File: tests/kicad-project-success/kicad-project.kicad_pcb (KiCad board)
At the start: 2 copper layers, 65 x 45 mm, 3 parts, among them SW101 SW_Push

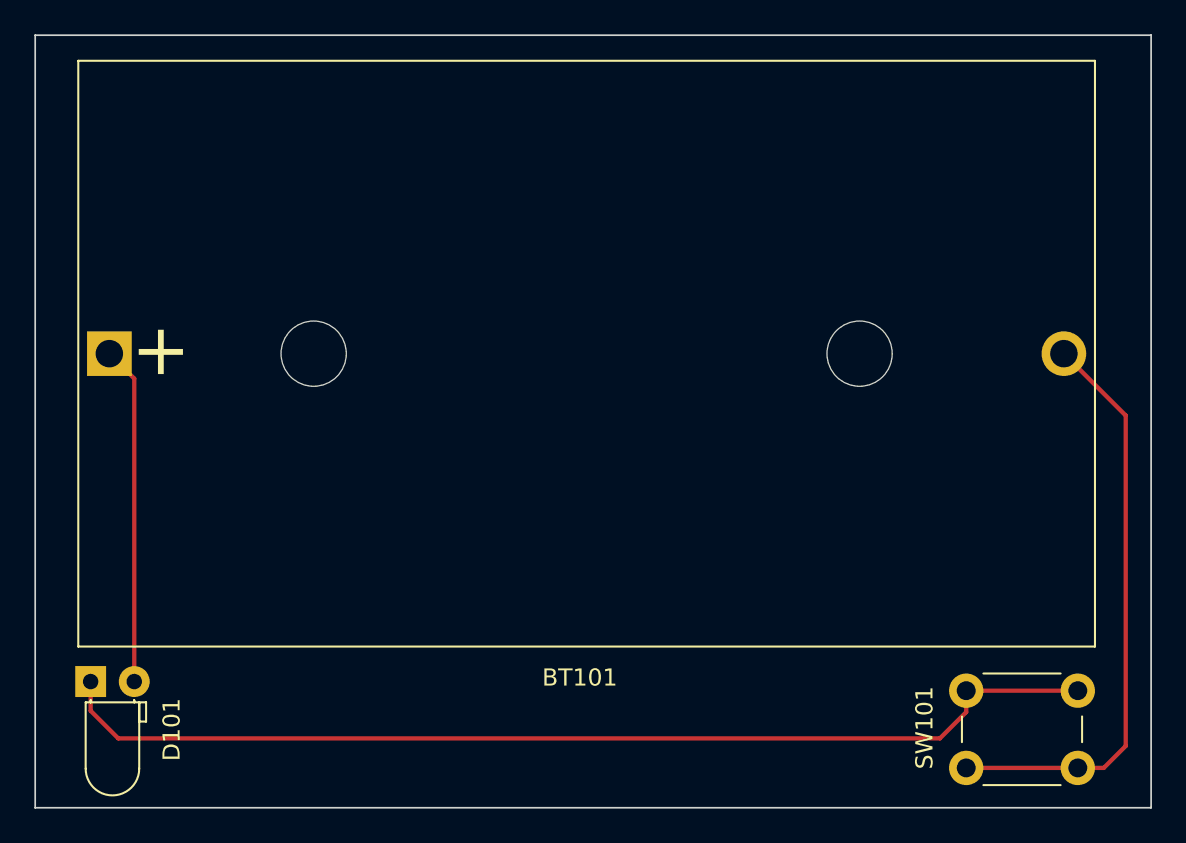
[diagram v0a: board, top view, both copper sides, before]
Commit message: Added footprint library support
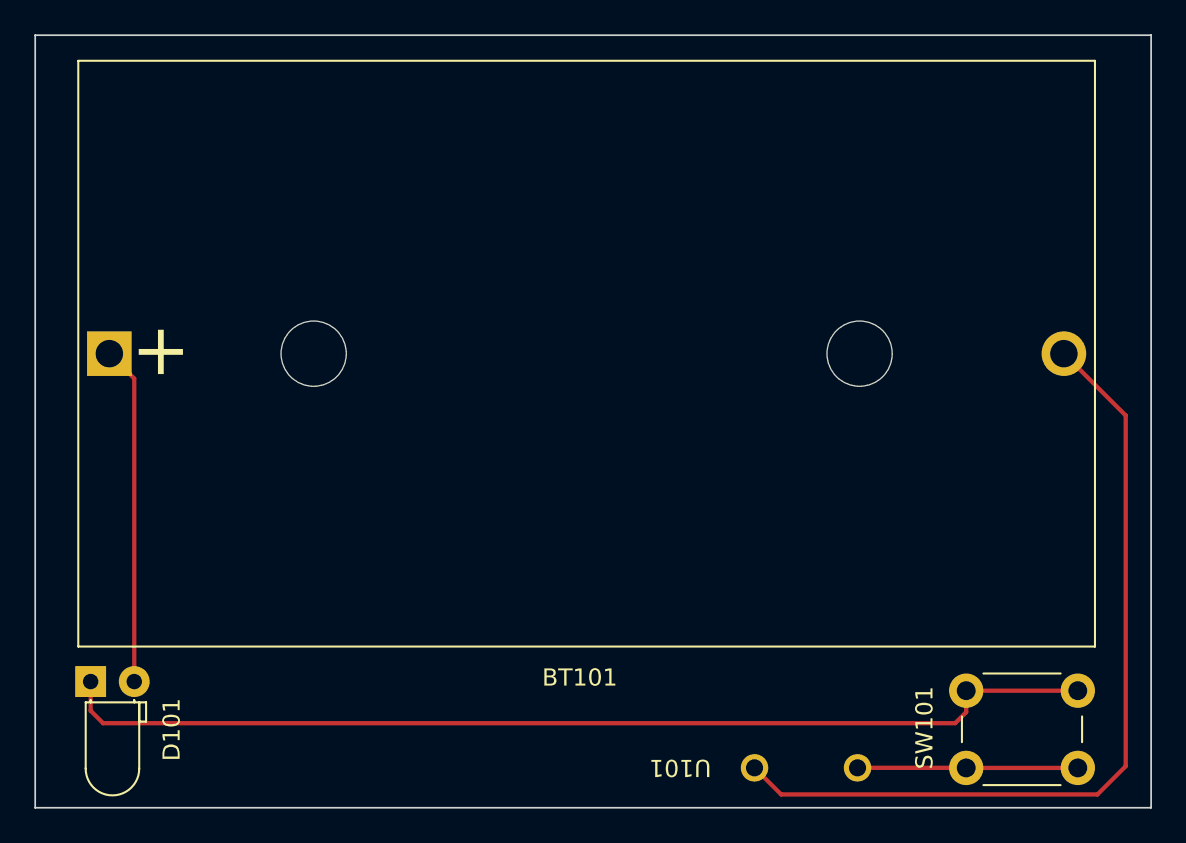
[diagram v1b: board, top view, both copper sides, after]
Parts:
- added U101: ~, test-fp-library:Line, F.Cu at (154.9, 107.7)
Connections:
- SW101 pad 2: GND -> Net-(U101-input)
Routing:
- net GND: track 34.2 -> 48.5 mm
- net Net-(U101-input): track 0.00 -> 12.4 mm
- net Net-(D101-K): track 61.8 -> 61.0 mm
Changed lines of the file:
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@@
 	(net 2 "GND")
 	(net 3 "Net-(D101-K)")
+	(net 4 "Net-(U101-input)")
 	(footprint "Battery:BatteryHolder_Bulgin_BX0036_1xC"
 		(layer "F.Cu")
@@
 			)
 		)
+		(sheetname "/")
 		(sheetfile "kicad-project.kicad_sch")
 		(attr through_hole)
@@
 			)
 		)
+		(property "Sim.Pins" "1=K 2=A"
+			(at 0 0 0)
+			(unlocked yes)
+			(layer "F.Fab")
+			(hide yes)
+			(effects
+				(font
+					(size 1 1)
+					(thickness 0.15)
+				)
+			)
+		)
+		(property ki_fp_filters "LED* LED_SMD:* LED_THT:*")
+		(sheetname "/")
 		(sheetfile "kicad-project.kicad_sch")
 		(attr through_hole)
@@
 			)
 		)
+		(sheetname "/")
 		(sheetfile "kicad-project.kicad_sch")
 		(attr through_hole)
@@
 			(layers "*.Cu" "*.Mask")
 			(remove_unused_layers no)
-			(net 2 "GND")
+			(net 4 "Net-(U101-input)")
 			(pinfunction "2")
 			(pintype "passive")
@@
 			(layers "*.Cu" "*.Mask")
 			(remove_unused_layers no)
-			(net 2 "GND")
+			(net 4 "Net-(U101-input)")
 			(pinfunction "2")
 			(pintype "passive")
@@
 			)
 		)
+	)
+	(footprint "test-fp-library:Line"
+		(layer "F.Cu")
+		(at 154.9 107.675 180)
+		(property "Reference" "U101"
+			(at 7.325 0 180)
+			(unlocked yes)
+			(layer "F.SilkS")
+			(effects
+				(font
+					(size 1 1)
+					(thickness 0.1)
+				)
+			)
+		)
+		(property "Value" "~"
+			(at 0 2.625 180)
+			(unlocked yes)
+			(layer "F.Fab")
+			(effects
+				(font
+					(size 1 1)
+					(thickness 0.15)
+				)
+			)
+		)
+		(property "Datasheet" ""
+			(at 0 3 180)
+			(unlocked yes)
+			(layer "F.Fab")
+			(hide yes)
+			(effects
+				(font
+					(size 1 1)
+					(thickness 0.15)
+				)
+			)
+		)
+		(property "Description" ""
+			(at 0 3 180)
+			(unlocked yes)
+			(layer "F.Fab")
+			(hide yes)
+			(effects
+				(font
+					(size 1 1)
+					(thickness 0.15)
+				)
+			)
+		)
+		(sheetname "/")
+		(sheetfile "kicad-project.kicad_sch")
+		(attr smd)
+		(fp_rect
+			(start -5 -2)
+			(end 5 2)
+			(stroke
+				(width 0.05)
+				(type default)
+			)
+			(fill no)
+			(layer "F.CrtYd")
+		)
+		(fp_text user "${REFERENCE}"
+			(at 0 3.625 180)
+			(unlocked yes)
+			(layer "F.Fab")
+			(effects
+				(font
+					(size 1 1)
+					(thickness 0.15)
+				)
+			)
+		)
+		(pad "1" thru_hole circle
+			(at -3 0 180)
+			(size 1.6 1.6)
+			(drill 1)
+			(layers "*.Cu" "*.Mask")
+			(remove_unused_layers no)
+			(net 4 "Net-(U101-input)")
+			(pinfunction "input")
+			(pintype "passive")
+		)
+		(pad "2" thru_hole circle
+			(at 3 0 180)
+			(size 1.6 1.6)
+			(drill 1)
+			(layers "*.Cu" "*.Mask")
+			(remove_unused_layers no)
+			(net 2 "GND")
+			(pinfunction "output")
+			(pintype "passive")
+		)
+		(embedded_fonts no)
 	)
 	(gr_line
@@
 	)
 	(segment
-		(start 164.23 107.68)
-		(end 170.73 107.68)
+		(start 171.875 109.225)
+		(end 173.52 107.58)
 		(width 0.25)
 		(layer "F.Cu")
@@
 	)
 	(segment
-		(start 173.52 106.4)
+		(start 153.45 109.225)
+		(end 171.875 109.225)
+		(width 0.25)
+		(layer "F.Cu")
+		(net 2)
+	)
+	(segment
+		(start 173.52 107.58)
 		(end 173.52 87.15)
 		(width 0.25)
@@
 	)
 	(segment
-		(start 172.24 107.68)
-		(end 173.52 106.4)
+		(start 151.9 107.675)
+		(end 153.45 109.225)
 		(width 0.25)
 		(layer "F.Cu")
@@
 	)
 	(segment
-		(start 170.73 107.68)
-		(end 172.24 107.68)
-		(width 0.25)
-		(layer "F.Cu")
-		(net 2)
+		(start 163.585 105.075)
+		(end 164.23 104.43)
+		(width 0.25)
+		(layer "F.Cu")
+		(net 3)
+	)
+	(segment
+		(start 113.23 104.35)
+		(end 113.955 105.075)
+		(width 0.25)
+		(layer "F.Cu")
+		(net 3)
+	)
+	(segment
+		(start 113.955 105.075)
+		(end 163.585 105.075)
+		(width 0.25)
+		(layer "F.Cu")
+		(net 3)
+	)
+	(segment
+		(start 164.23 104.43)
+		(end 164.23 103.18)
+		(width 0.25)
+		(layer "F.Cu")
+		(net 3)
+	)
+	(segment
+		(start 164.23 103.18)
+		(end 170.73 103.18)
+		(width 0.25)
+		(layer "F.Cu")
+		(net 3)
 	)
 	(segment
@@
 	)
 	(segment
-		(start 114.84 105.96)
-		(end 162.7 105.96)
-		(width 0.25)
-		(layer "F.Cu")
-		(net 3)
-	)
-	(segment
-		(start 113.23 104.35)
-		(end 114.84 105.96)
-		(width 0.25)
-		(layer "F.Cu")
-		(net 3)
-	)
-	(segment
-		(start 164.23 103.18)
-		(end 170.73 103.18)
-		(width 0.25)
-		(layer "F.Cu")
-		(net 3)
-	)
-	(segment
-		(start 162.7 105.96)
-		(end 164.23 104.43)
-		(width 0.25)
-		(layer "F.Cu")
-		(net 3)
-	)
-	(segment
-		(start 164.23 104.43)
-		(end 164.23 103.18)
-		(width 0.25)
-		(layer "F.Cu")
-		(net 3)
+		(start 157.9 107.675)
+		(end 163.774 107.675)
+		(width 0.25)
+		(layer "F.Cu")
+		(net 4)
+	)
+	(segment
+		(start 170.73 107.68)
+		(end 164.23 107.68)
+		(width 0.25)
+		(layer "F.Cu")
+		(net 4)
+	)
+	(segment
+		(start 163.774 107.675)
+		(end 163.779 107.68)
+		(width 0.25)
+		(layer "F.Cu")
+		(net 4)
 	)
 	(embedded_fonts no)
